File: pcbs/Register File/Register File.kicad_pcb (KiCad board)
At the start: 4 copper layers, 209 parts, among them U1001 74HC138, U201 74HCT574, U202 74HC245, U203 74HC245, U204 74HC245, U301 74HCT574, U302 74HC245, U303 74HC245, U304 74HC245, U401 74HCT574, U402 74HC245, U403 74HC245, U404 74HC245, U501 74HCT574, U502 74HC245, U503 74HC245, U504 74HC245, U601 74HCT574, U602 74HC245, U603 74HC245, U604 74HC245, U701 74HCT574, U702 74HC245, U703 74HC245, U704 74HC245, U801 74HCT574, U802 74HC245, U803 74HC245, U804 74HC245, U901 74HCT574, U902 74HC245, U903 74HC245, U904 74HC245

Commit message: More work
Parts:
- added R1001: 220k, Resistor_SMD:R_0603_1608Metric, F.Cu at (45.7, 30.5)
- added R1002: 220k, Resistor_SMD:R_0603_1608Metric, F.Cu at (45.7, 33.0)
- added R1003: 220k, Resistor_SMD:R_0603_1608Metric, F.Cu at (45.7, 35.6)
- added R1004: 220k, Resistor_SMD:R_0603_1608Metric, F.Cu at (45.7, 38.1)
- added R1005: 220k, Resistor_SMD:R_0603_1608Metric, F.Cu at (45.7, 40.6)
- added R1006: 220k, Resistor_SMD:R_0603_1608Metric, F.Cu at (45.7, 43.2)
- added R1007: 220k, Resistor_SMD:R_0603_1608Metric, F.Cu at (45.7, 45.7)
- added R1008: 220k, Resistor_SMD:R_0603_1608Metric, F.Cu at (45.7, 48.3)
- added U1002: 74HC138, Package_DIP:DIP-16_W7.62mm_Socket, F.Cu at (43.2, 74.9)
- added U1003: 74HC138, Package_DIP:DIP-16_W7.62mm_Socket, F.Cu at (43.2, 92.7)
- added U1004: 74HC138, Package_DIP:DIP-16_W7.62mm_Socket, F.Cu at (17.8, 25.4)
- added U1005: 74HC540, Package_DIP:DIP-20_W7.62mm_Socket, F.Cu at (33.0, 25.4)
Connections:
- net /Register 0/~{B_{Enable}} renamed /Selectors/~{B_{select}}0
- net /Register 0/~{C_{Enable}} renamed /Selectors/~{C_{select}}0
- net /Register 1/~{B_{Enable}} renamed /Selectors/~{B_{select}}1
- net /Register 1/~{C_{Enable}} renamed /Selectors/~{C_{select}}1
- net /Register 2/~{B_{Enable}} renamed /Selectors/~{B_{select}}2
- net /Register 2/~{C_{Enable}} renamed /Selectors/~{C_{select}}2
- net /Register 3/~{B_{Enable}} renamed /Selectors/~{B_{select}}3
- net /Register 3/~{C_{Enable}} renamed /Selectors/~{C_{select}}3
- net /Register 4/~{B_{Enable}} renamed /Selectors/~{B_{select}}4
- net /Register 4/~{C_{Enable}} renamed /Selectors/~{C_{select}}4
- net /Register 5/~{B_{Enable}} renamed /Selectors/~{B_{select}}5
- net /Register 5/~{C_{Enable}} renamed /Selectors/~{C_{select}}5
- net /Register 6/~{B_{Enable}} renamed /Selectors/~{B_{select}}6
- net /Register 6/~{C_{Enable}} renamed /Selectors/~{C_{select}}6
- net /Register 7/~{B_{Enable}} renamed /Selectors/~{B_{select}}7
- net /Register 7/~{C_{Enable}} renamed /Selectors/~{C_{select}}7
- U201 pad 11: /Register 0/C_{write} -> /Selectors/C_{Write}0
- U301 pad 11: /Register 1/C_{write} -> /Selectors/C_{Write}1
- U401 pad 11: /Register 2/C_{write} -> /Selectors/C_{Write}2
- U501 pad 11: /Register 3/C_{write} -> /Selectors/C_{Write}3
- U601 pad 11: /Register 4/C_{write} -> /Selectors/C_{Write}4
- U701 pad 11: /Register 5/C_{write} -> /Selectors/C_{Write}5
- U801 pad 11: /Register 6/C_{write} -> /Selectors/C_{Write}6
- U901 pad 11: /Register 7/C_{write} -> /Selectors/C_{Write}7
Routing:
- net /Selectors/C_{Write}7: track 0.00 -> 245.9 mm, vias 0 -> 1
- net /Selectors/C_{Write}6: track 0.00 -> 219.5 mm, vias 0 -> 1
- net /Selectors/C_{Write}5: track 0.00 -> 193.1 mm, vias 0 -> 1
- net /Selectors/C_{Write}4: track 0.00 -> 166.7 mm, vias 0 -> 1
- net /Selectors/C_{Write}3: track 0.00 -> 140.3 mm, vias 0 -> 1
- net /Selectors/C_{Write}2: track 0.00 -> 113.9 mm, vias 0 -> 1
- net /Selectors/C_{Write}1: track 0.00 -> 87.4 mm, vias 0 -> 1
- net /Selectors/C_{Write}0: track 0.00 -> 61.0 mm, vias 0 -> 1
- net /Selectors/~{B_{select}}6: track 169.4 -> 221.3 mm
- net /Selectors/~{C_{select}}6: track 169.9 -> 221.3 mm
- net /Selectors/~{B_{select}}5: track 143.5 -> 192.3 mm
- net /Selectors/~{C_{select}}5: track 144.0 -> 192.3 mm
- net /Selectors/~{B_{select}}4: track 117.6 -> 163.4 mm
- net /Selectors/~{C_{select}}4: track 118.1 -> 163.4 mm
- net /Selectors/~{B_{select}}3: track 91.7 -> 134.4 mm
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
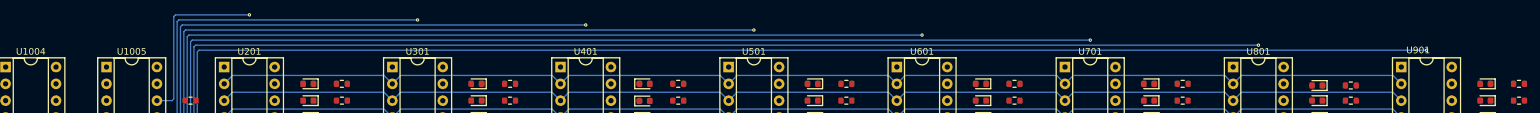
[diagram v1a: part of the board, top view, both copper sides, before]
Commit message: Adding some capacitors
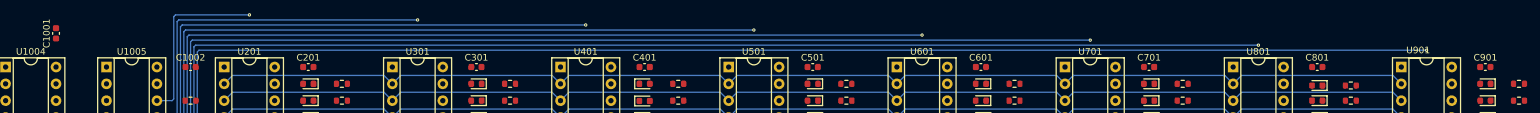
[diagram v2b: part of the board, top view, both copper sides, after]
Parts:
- added C1001: 100n, Capacitor_SMD:C_0603_1608Metric, F.Cu at (25.4, 20.3)
- added C1002: 100n, Capacitor_SMD:C_0603_1608Metric, F.Cu at (45.7, 25.4)
- added C201: 100n, Capacitor_SMD:C_0603_1608Metric, F.Cu at (63.5, 25.4)
- added C301: 100n, Capacitor_SMD:C_0603_1608Metric, F.Cu at (88.9, 25.4)
- added C401: 100n, Capacitor_SMD:C_0603_1608Metric, F.Cu at (114.3, 25.4)
- added C501: 100n, Capacitor_SMD:C_0603_1608Metric, F.Cu at (139.7, 25.4)
- added C601: 100n, Capacitor_SMD:C_0603_1608Metric, F.Cu at (165.1, 25.4)
- added C701: 100n, Capacitor_SMD:C_0603_1608Metric, F.Cu at (190.5, 25.4)
- added C801: 100n, Capacitor_SMD:C_0603_1608Metric, F.Cu at (215.9, 25.4)
- added C901: 100n, Capacitor_SMD:C_0603_1608Metric, F.Cu at (241.3, 25.4)

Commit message: Lots of LEDs
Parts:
- added D1001: YELLOW, LED_SMD:LED_0603_1608Metric, F.Cu at (58.4, 22.9)
- added D1002: YELLOW, LED_SMD:LED_0603_1608Metric, F.Cu at (83.8, 22.9)
- added D1003: YELLOW, LED_SMD:LED_0603_1608Metric, F.Cu at (109.2, 22.9)
- added D1004: YELLOW, LED_SMD:LED_0603_1608Metric, F.Cu at (134.6, 22.9)
- added D1005: YELLOW, LED_SMD:LED_0603_1608Metric, F.Cu at (160.0, 22.9)
- added D1006: YELLOW, LED_SMD:LED_0603_1608Metric, F.Cu at (185.4, 22.9)
- added D1007: YELLOW, LED_SMD:LED_0603_1608Metric, F.Cu at (210.8, 22.9)
- added D1008: YELLOW, LED_SMD:LED_0603_1608Metric, F.Cu at (236.2, 22.9)
- added R1009: 4k7, Resistor_SMD:R_0603_1608Metric, F.Cu at (50.8, 22.9)
- added R1010: 4k7, Resistor_SMD:R_0603_1608Metric, F.Cu at (76.2, 22.9)
- added R1011: 4k7, Resistor_SMD:R_0603_1608Metric, F.Cu at (101.6, 22.9)
- added R1012: 4k7, Resistor_SMD:R_0603_1608Metric, F.Cu at (127.0, 22.9)
- added R1013: 4k7, Resistor_SMD:R_0603_1608Metric, F.Cu at (152.4, 22.9)
- added R1014: 4k7, Resistor_SMD:R_0603_1608Metric, F.Cu at (177.7, 22.9)
- added R1015: 4k7, Resistor_SMD:R_0603_1608Metric, F.Cu at (203.2, 22.9)
- added R1016: 4k7, Resistor_SMD:R_0603_1608Metric, F.Cu at (228.6, 22.9)
- moved C1001 6.35 mm to (29.2, 25.4), turned to 0 degrees
- moved D801 0.25 mm to (215.9, 27.9)
- moved D807 0.25 mm to (215.9, 43.2)
- moved R801 0.25 mm to (221.0, 27.9)
- moved R807 0.25 mm to (221.0, 43.2)
- moved D402 0.05 mm to (114.3, 30.5), turned to 180 degrees
- turned D401 to 180 degrees
- turned D403 to 180 degrees
- turned D404 to 180 degrees
- turned D405 to 180 degrees
- turned D406 to 180 degrees
- turned D407 to 180 degrees
- turned D408 to 180 degrees
- turned R401 to 180 degrees
- turned R402 to 180 degrees
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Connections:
- net Net-(U1004-~{Y0}) renamed /Selectors/W0
- net Net-(U1004-~{Y1}) renamed /Selectors/W1
- net Net-(U1004-~{Y2}) renamed /Selectors/W2
- net Net-(U1004-~{Y3}) renamed /Selectors/W3
- net Net-(U1004-~{Y4}) renamed /Selectors/W4
- net Net-(U1004-~{Y5}) renamed /Selectors/W5
- net Net-(U1004-~{Y6}) renamed /Selectors/W6
- net Net-(U1004-~{Y7}) renamed /Selectors/W7
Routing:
- net /Selectors/W7: track 0.00 -> 220.7 mm, vias 0 -> 1
- net /Selectors/W6: track 0.00 -> 201.0 mm, vias 0 -> 1
- net /Selectors/W5: track 0.00 -> 174.5 mm, vias 0 -> 1
- net /Selectors/W4: track 0.00 -> 148.1 mm, vias 0 -> 1
- net /Selectors/W3: track 0.00 -> 121.7 mm, vias 0 -> 2
- net /Selectors/W2: track 0.00 -> 95.3 mm, vias 0 -> 1
- net /Selectors/W1: track 0.00 -> 68.9 mm, vias 0 -> 1
- net +5V: track 0.00 -> 64.7 mm
- net /Selectors/W0: track 0.00 -> 41.4 mm, vias 0 -> 1
- net Net-(D1008-K): track 0.00 -> 6.64 mm
- net Net-(D1006-K): track 0.00 -> 6.07 mm
- net Net-(D1004-K): track 0.00 -> 6.01 mm
- net Net-(D1003-K): track 0.00 -> 6.01 mm
- net Net-(D1001-K): track 0.00 -> 6.01 mm
- net Net-(D1007-K): track 0.00 -> 6.01 mm
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
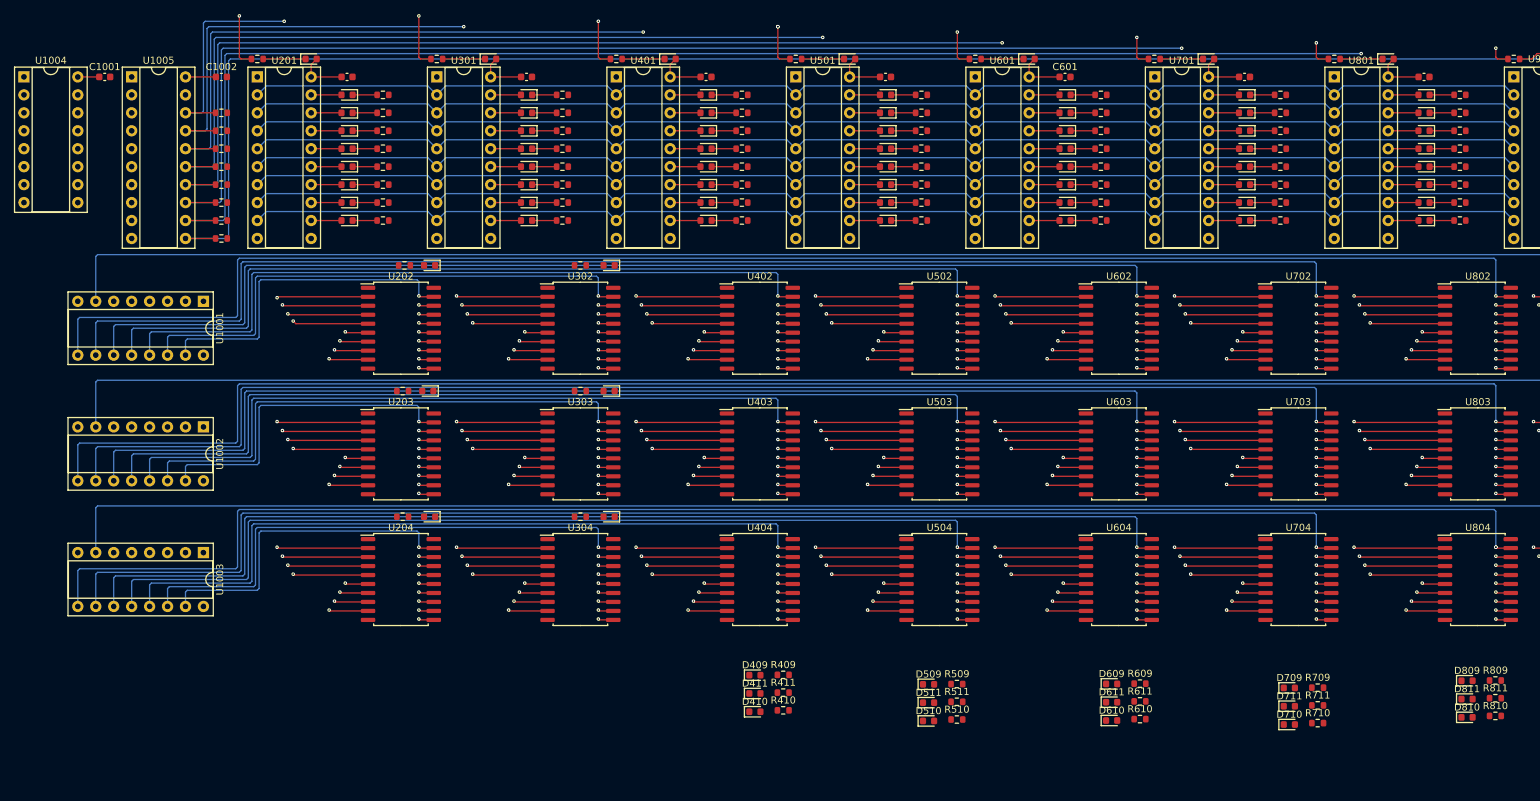
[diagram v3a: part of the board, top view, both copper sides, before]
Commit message: More control logic
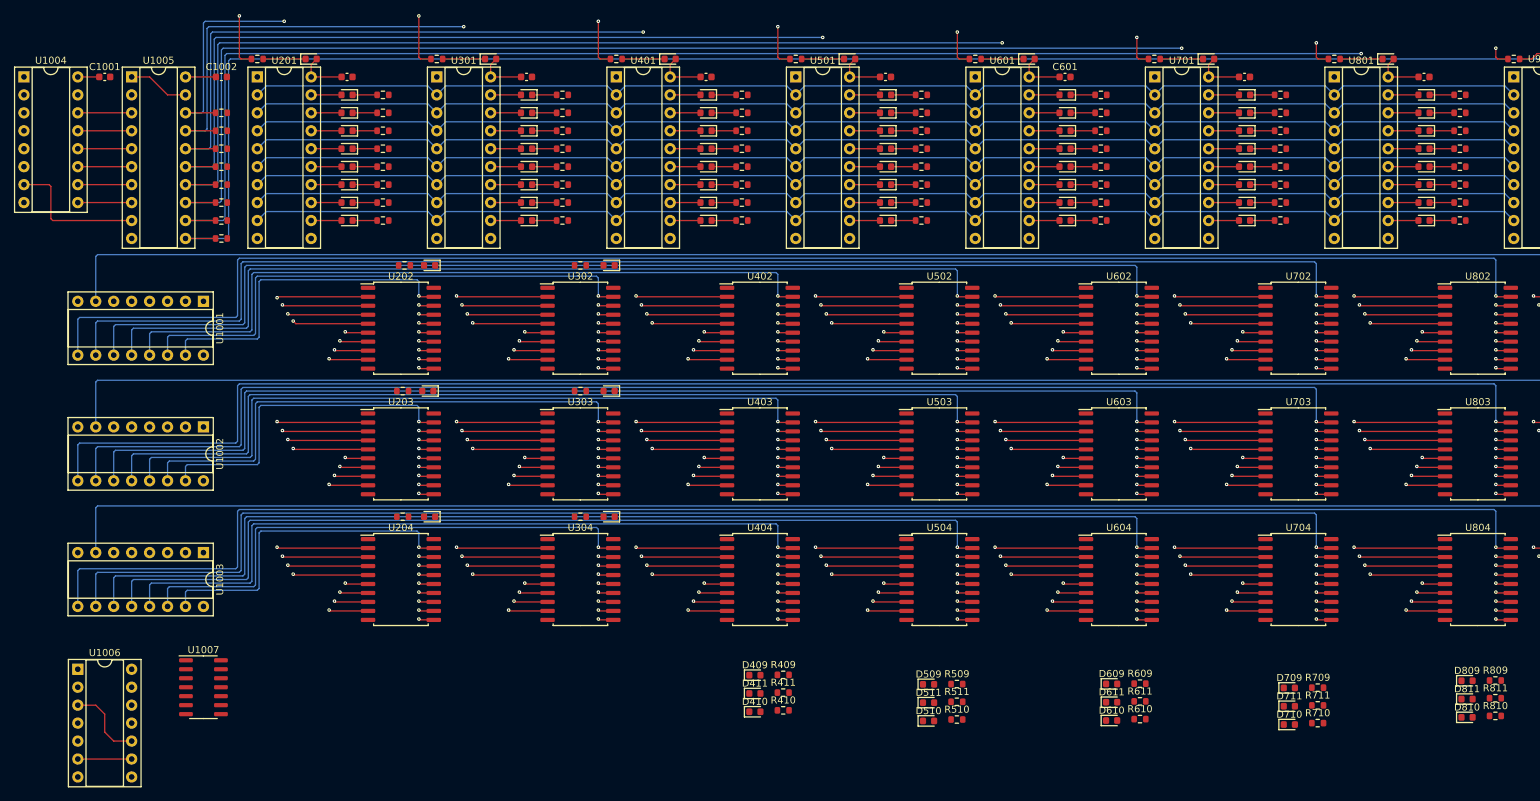
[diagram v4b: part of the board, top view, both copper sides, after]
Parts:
- added U1006: 74HC32, Package_DIP:DIP-14_W7.62mm_Socket, F.Cu at (25.4, 109.2)
- added U1007: 74HC14, Package_SO:SOIC-14_3.9x8.7mm_P1.27mm, F.Cu at (43.2, 111.8)
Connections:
- U1001 pad 4: unconnected-(U1001-~{E0}-Pad4) -> /Selectors/~{Active}
- U1002 pad 4: unconnected-(U1002-~{E0}-Pad4) -> /Selectors/~{Active}
- U1003 pad 4: unconnected-(U1003-~{E0}-Pad4) -> /Selectors/~{Active}
- U1003 pad 5: unconnected-(U1003-~{E1}-Pad5) -> /Selectors/C_{W}/~{C_{R}}
- U1004 pad 4: unconnected-(U1004-~{E0}-Pad4) -> /Selectors/~{Active}
- U1004 pad 6: unconnected-(U1004-E2-Pad6) -> /Selectors/C_{W}/~{C_{R}}
- U1005 pad 1: unconnected-(U1005-G1-Pad1) -> /Selectors/~{Execute}
- U1005 pad 19: unconnected-(U1005-G2-Pad19) -> /Selectors/~{Execute}
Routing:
- net /Selectors/~{Active}: track 0.00 -> 96.9 mm
- net /Selectors/R_{C}0: track 0.00 -> 92.3 mm
- net /Selectors/~{Execute}: track 0.00 -> 90.5 mm
- net /Selectors/R_{C}1: track 0.00 -> 87.2 mm
- net /Selectors/R_{C}2: track 0.00 -> 82.1 mm
- net /Selectors/C_{W}/~{C_{R}}: track 0.00 -> 74.5 mm
- net /Selectors/W7: track 220.7 -> 243.9 mm
- net Net-(U1006-Pad10): track 0.00 -> 11.2 mm
- net Net-(U1006-Pad6): track 0.00 -> 7.62 mm
- net /Selectors/W6: track 201.0 -> 208.6 mm
- net /Selectors/W5: track 174.5 -> 182.1 mm
- net /Selectors/W4: track 148.1 -> 155.8 mm
- net /Selectors/W3: track 121.7 -> 129.3 mm, vias 2 -> 1
- net /Selectors/W2: track 95.3 -> 102.9 mm
- net /Selectors/W1: track 68.9 -> 76.5 mm
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
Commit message: Routing the connector Pt 1 of n
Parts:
- added J101: Conn_02x20_Odd_Even, Connector_PinHeader_2.54mm:PinHeader_2x20_P2.54mm_Vertical, F.Cu at (127.0, 121.9)
- moved D710 64.4 mm to (202.2, 52.8), turned to 180 degrees
- moved R710 64.1 mm to (198.1, 52.8), turned to 180 degrees
- moved D510 63.9 mm to (151.4, 52.8), turned to 180 degrees
- moved D610 63.8 mm to (176.8, 52.8), turned to 180 degrees
- moved R510 63.5 mm to (147.3, 52.8), turned to 180 degrees
- moved R610 63.5 mm to (172.7, 52.8), turned to 180 degrees
- moved D810 63.4 mm to (227.6, 52.8), turned to 180 degrees
- moved R810 63.0 mm to (223.5, 52.8), turned to 180 degrees
- moved R910 62.3 mm to (248.9, 52.8), turned to 180 degrees
- moved D910 62.2 mm to (253.0, 52.8), turned to 180 degrees
- moved D409 57.4 mm to (126.0, 52.8), turned to 180 degrees
- moved R409 57.3 mm to (121.9, 52.8), turned to 180 degrees
- moved D410 44.9 mm to (126.0, 70.6), turned to 180 degrees
- moved R410 44.5 mm to (121.9, 70.6), turned to 180 degrees
- moved D711 44.2 mm to (202.2, 70.6), turned to 180 degrees
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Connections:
- U1006 pad 12: unconnected-(U1006-Pad12) -> GND
- U1006 pad 13: unconnected-(U1006-Pad13) -> GND
- U1007 pad 11: unconnected-(U1007-Pad11) -> GND
- U1007 pad 13: unconnected-(U1007-Pad13) -> GND
- U1007 pad 5: unconnected-(U1007-Pad5) -> GND
- U1007 pad 9: unconnected-(U1007-Pad9) -> GND
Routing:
- net /Register 0/C0: track 384.7 -> 532.5 mm, vias 8 -> 9
- net /Register 0/C1: track 384.7 -> 528.9 mm, vias 8 -> 9
- net /Register 0/C2: track 384.7 -> 525.4 mm, vias 8 -> 9
- net /Register 0/C3: track 384.7 -> 521.8 mm, vias 8 -> 9
- net /Register 0/C4: track 386.8 -> 520.3 mm, vias 8 -> 9
- net /Register 0/C5: track 386.8 -> 516.8 mm, vias 8 -> 9
- net /Register 0/C6: track 386.8 -> 513.2 mm, vias 8 -> 9
- net /Register 0/C7: track 386.8 -> 509.9 mm, vias 8 -> 9
- net /Register 0/A0: track 199.5 -> 281.1 mm
- net /Register 0/A1: track 199.5 -> 277.3 mm
- net /Register 0/A2: track 199.5 -> 273.5 mm
- net /Register 0/A3: track 199.5 -> 269.7 mm
- net /Register 0/A4: track 201.6 -> 268.0 mm
- net /Register 0/B0: track 199.5 -> 263.3 mm
- net /Register 0/A5: track 201.6 -> 264.2 mm
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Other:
- board text added: "JLCJLCJLCJLC"
- board text added: "RGE2023"
